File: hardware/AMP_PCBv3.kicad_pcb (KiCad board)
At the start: 2 copper layers, 70 x 82.5 mm, 86 parts, among them J1 Input_PWR, J2 VESC_PPM, J3 VESC_COMM, J4 LED_Header, J5 USB_B_Mini, J6 STEERING, M1 Fan_PC_3pin, M2 Brake, M3 Fan_PC_3pin, M4 Fan_PC_3pin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

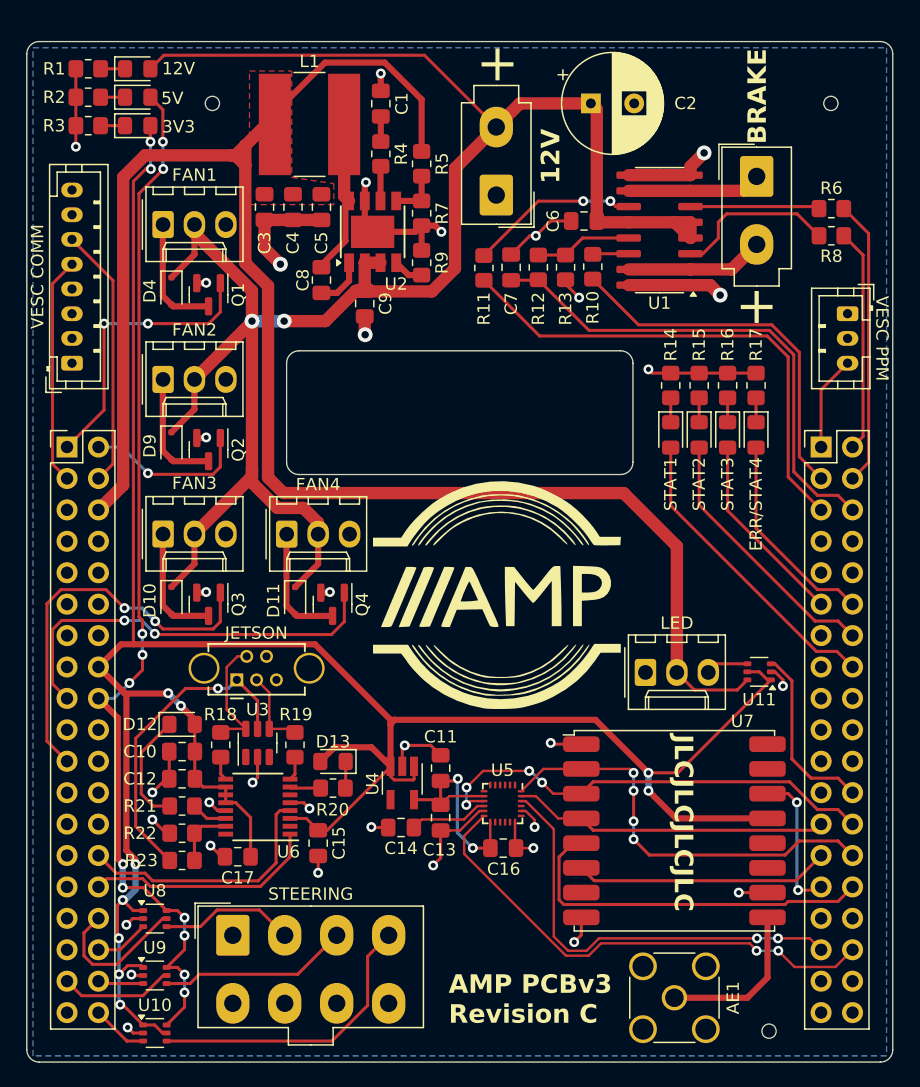
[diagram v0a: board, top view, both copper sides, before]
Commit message: Fix #6
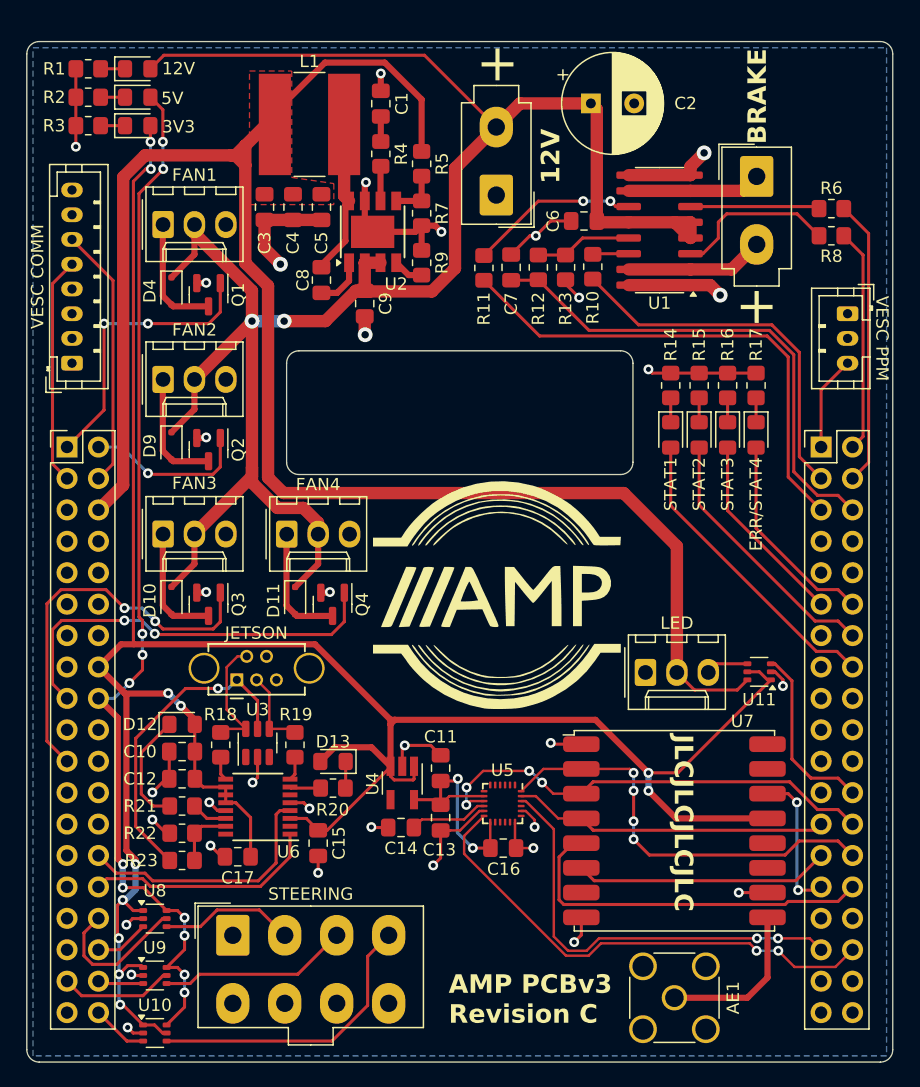
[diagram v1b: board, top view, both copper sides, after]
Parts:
- removed H1, H2, H3: Tooling Hole, AMP_Custom:JLCPCB_Tooling_Hole
